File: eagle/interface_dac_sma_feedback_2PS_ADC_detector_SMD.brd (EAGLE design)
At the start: 158.8 x 119.4 mm, 26 parts

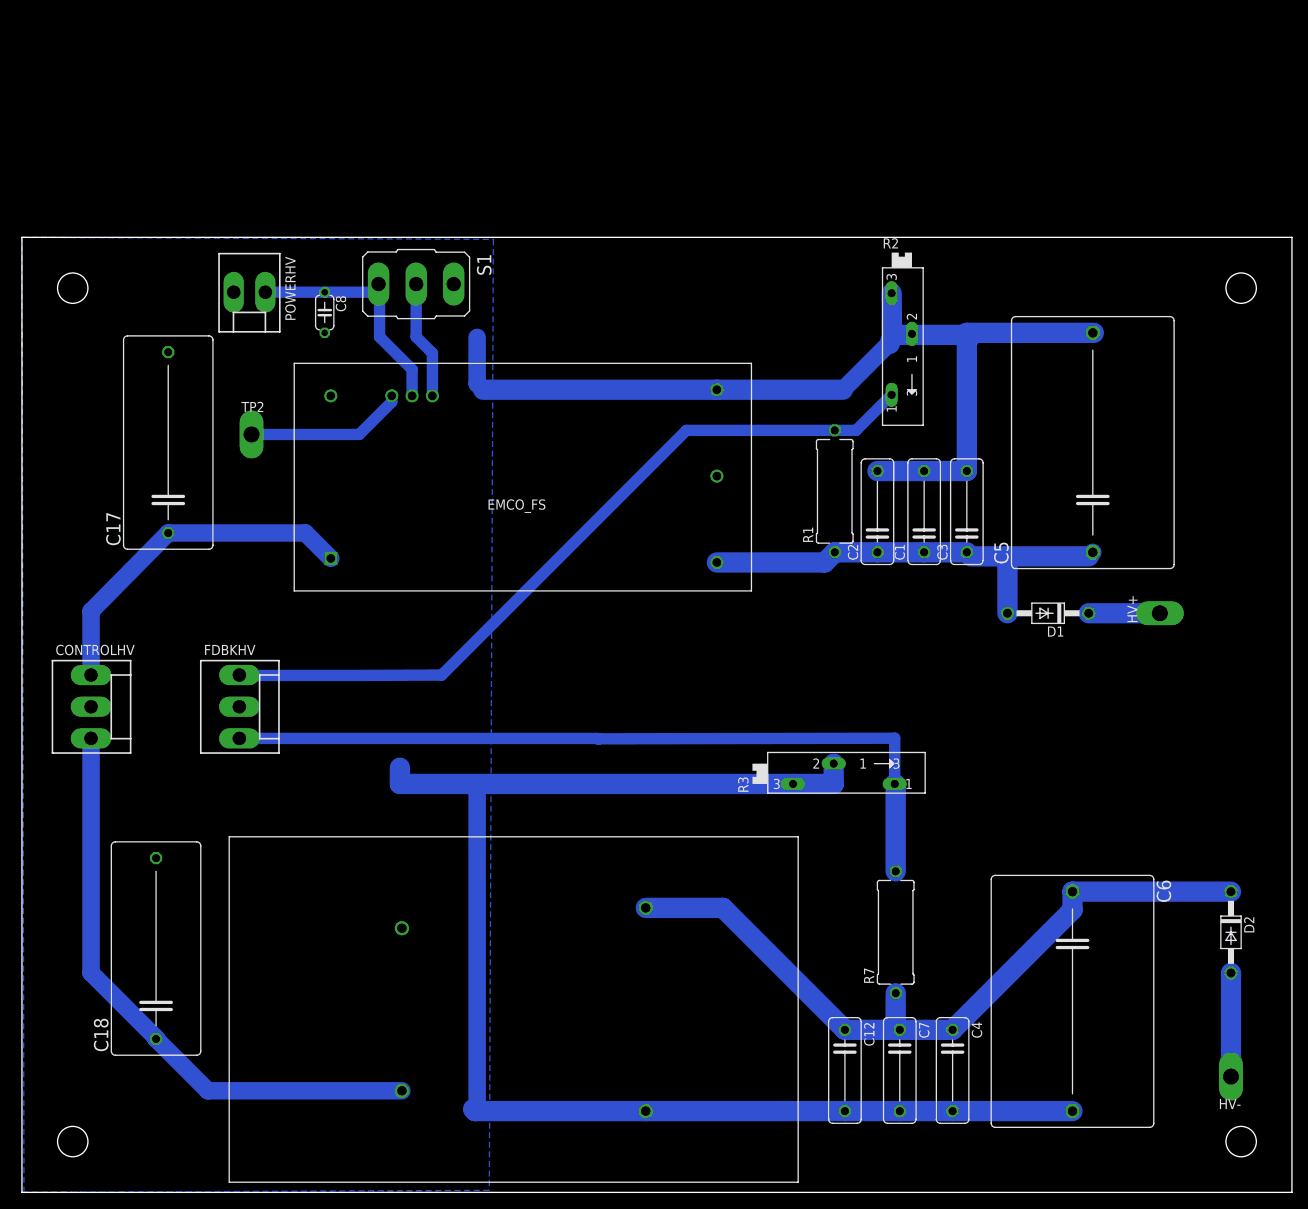
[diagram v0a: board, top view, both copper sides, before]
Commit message: Square wave one side/dc other
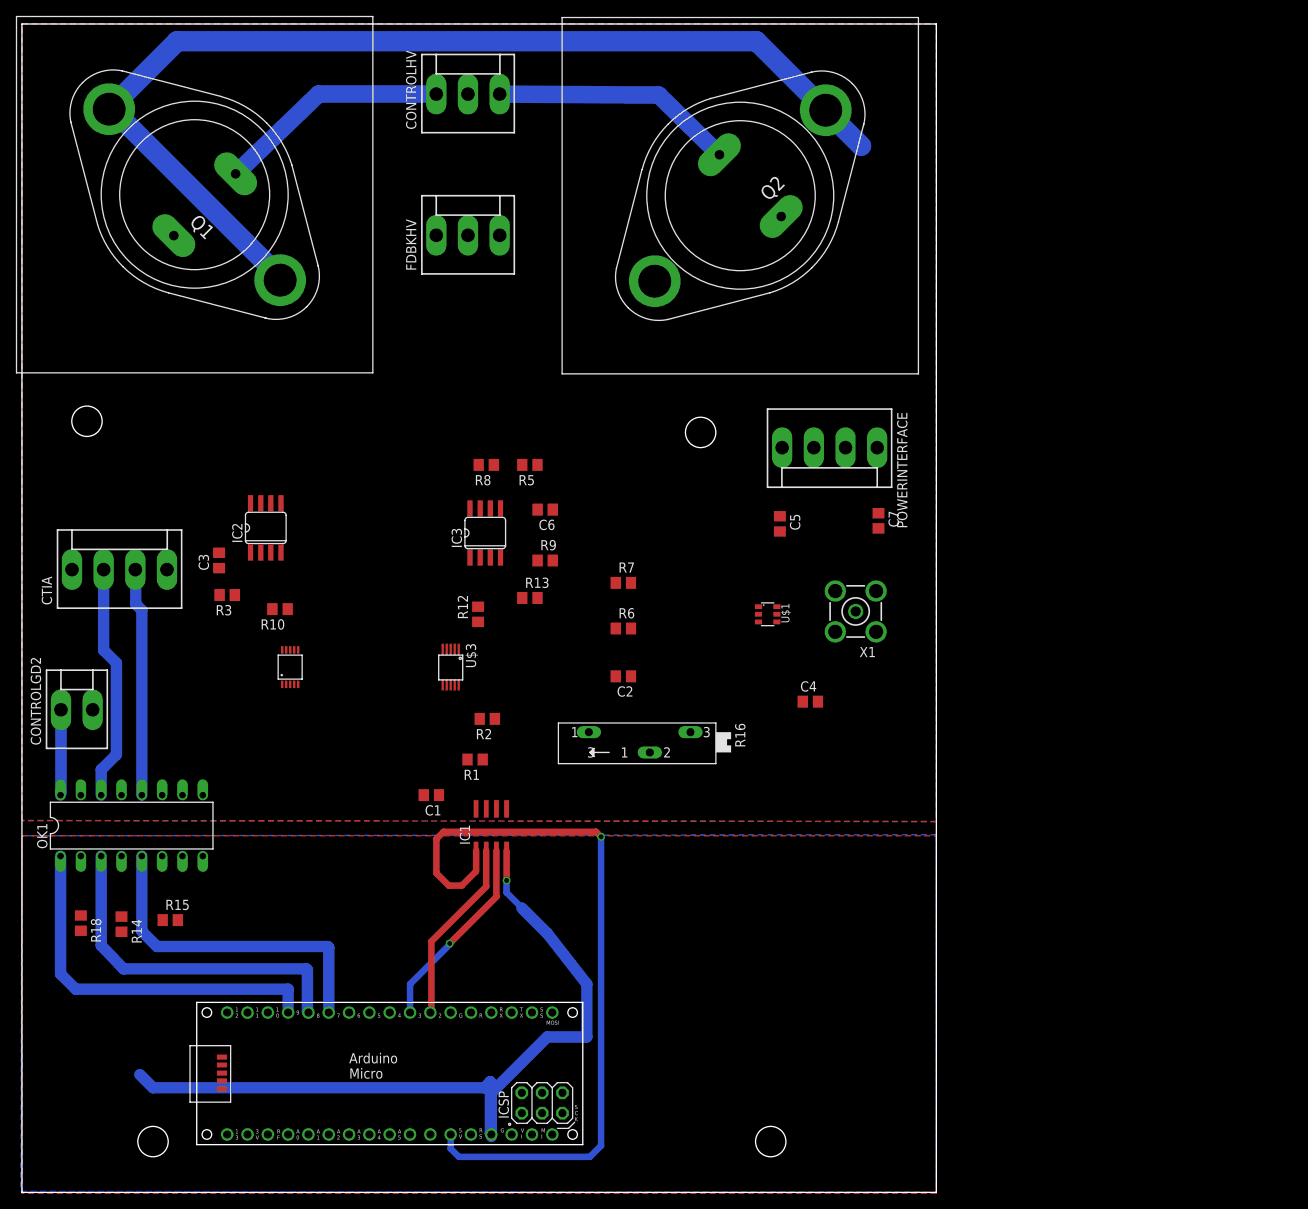
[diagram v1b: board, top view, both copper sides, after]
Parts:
- removed C12: .01u, rcl:C102-043X133
- removed C17, C18: .1u, rcl:C225-113X268
- removed C8: 10n, rcl:C050-024X044
- removed D1, D2: 1N4004, diode:DO41-10
- removed HV+, HV-: TPPAD1-20Y, testpad:P1-20Y
- removed POWERHV: (no value), con-molex:KK-156-2
- removed S1: (no value), switch:M9040P
- removed TP2: PTR1PAD1-20Y, testpad:P1-20Y
- added CONTROLGD2: (no value), con-molex:KK-156-2
- added CTIA, POWERINTERFACE: (no value), con-molex:KK-156-4
- added IC1: ISO1540SMD, texas:SOIC8
- added IC2, IC3: LT1352SA, linear-technology:SO08
- added OK1: PS2501", optocoupler:DIL16
- added PCB1: ARDUINO_MICRO, E14_Arduino_published:ARDUINO_MICRO
- added Q1, Q2: 2N3055, transistor-npn:TO3
- added R10, R12, R13, R6, R9: 10k, resistor:R0805
- added R14, R15, R18: 100, rcl:R0805
- added R16: 100k, pot:SP19L
- added R5, R8: 20k, resistor:R0805
- added U$3: ADS1015, texas:VSOP-10
- added X1: BU-SMA-V, con-coax:BU-SMA-V
- C1: value 1n -> 10n; device rcl:C102-043X133 -> rcl:C0805
- C2, C7: value 10p -> 10n; device rcl:C102-043X133 -> resistor:C0805
- C3: value .01u -> 10n; device rcl:C102-043X133 -> resistor:C0805
- C4: value 1n -> 10n; device rcl:C102-043X133 -> resistor:C0805
- C5, C6: value 1u -> 10n; device rcl:C275-205X316 -> resistor:C0805
- R1: value 2M -> 10k; device resistor:P0613/15 -> resistor:R0805
- R2, R3: value (none) -> 10k; device pot:SP19L -> resistor:R0805
- R7: value 2M -> 40k; device resistor:P0613/15 -> resistor:R0805
- U$1: value EMCO-FS10 -> LTC6992SMD; device dc-dc-converter:EMCO-FS -> linear-technology:SOT23-6
- U$2: value EMCO-F104PIN -> MCP4728; device dc-dc-converter:EMCO-F -> microchip:MSOP-10
- moved C3 93.7 mm to (24.6, 79.0)
- moved C6 90.1 mm to (65.4, 85.3), turned to 180 degrees
- moved CONTROLHV 89.9 mm to (55.8, 137.3), turned to 0 degrees
- moved R3 80.9 mm to (25.7, 74.7), turned to 180 degrees
- moved C1 71.1 mm to (51.2, 49.7), turned to 180 degrees
- moved R2 69.4 mm to (58.2, 59.2), turned to 180 degrees
- moved C7 68.8 mm to (107.1, 83.9)
- moved FDBKHV 65.5 mm to (55.8, 119.6), turned to 0 degrees
- moved U$1 59.3 mm to (93.2, 72.3), turned to 270 degrees
- moved R1 56.1 mm to (56.6, 54.1), turned to 180 degrees
- moved R7 55.4 mm to (75.2, 76.2), turned to 0 degrees
- moved U$2 54.8 mm to (33.5, 65.7), turned to 90 degrees
- moved C4 49.4 mm to (98.6, 61.3), turned to 0 degrees
- moved C5 40.4 mm to (94.7, 83.6), turned to 270 degrees
- moved C2 37.8 mm to (75.2, 64.5), turned to 180 degrees
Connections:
- removed net +5V: C8.1, POWERHV.1, S1.3, U$1.+5
- removed net N$10: TP2.TP, U$1.ALARM
- removed net N$15: C18.1, CONTROLHV.3, U$2.P$1
- new net +15V: C7.1, IC2.8, IC3.8, POWERINTERFACE.1, Q1.C, Q1.C/, Q2.C, Q2.C/
- new net -15V: C5.1, IC2.4, IC3.4, POWERINTERFACE.4
- new net A+5: IC1.1, PCB1.+5V
- new net AGND: IC1.4, PCB1.GND., R14.2, R15.2, R18.2
- new net CTIA: CTIA.4, U$3.AIN1
- new net D10: PCB1.D10
- new net D11: PCB1.D11
- new net D4: PCB1.D4
- new net D7: OK1.5, PCB1.D7
- new net D8: OK1.3, PCB1.D8
- new net ENSW2: CONTROLGD2.1, OK1.16
- new net N$12: R16.E, U$1.3
- new net N$14: IC3.7, R13.1, R8.2
- new net N$16: IC2.3, R10.2
- new net N$18: IC3.3, R12.2
- new net N$19: C3.2, IC2.1, Q1.B
- new net N$20: C6.1, R9.2
- new net N$21: C6.2, IC3.1, Q2.B
- new net N$23: IC3.6, R5.2, R8.1
- new net N$24: R10.1, U$2.P$9
- new net N$25: R12.1, U$2.P$7
- new net N$26: U$2.P$8
- new net N$7: OK1.2, R18.1
- new net PWM5: PCB1.D5
- new net PWM6: PCB1.D6
- new net PWM9: OK1.1, PCB1.D9
- new net RDBK1: FDBKHV.1, IC2.2, R3.1, U$3.AIN0
- new net RDBK3: IC3.2, R13.2, R9.1, U$3.AIN2
- new net RDBK4: C2.1, R6.2, R7.2, U$1.1, U$3.AIN3
- new net RESET: CTIA.3, OK1.12
- new net SAMPLE: CTIA.2, OK1.14
- new net SCL: IC1.3, PCB1.D3
- new net SCL_OUT: IC1.6, R2.1, U$2.P$2, U$3.SCL
- new net SDA: IC1.2, PCB1.D2
- new net SDA_OUT: IC1.7, R1.1, U$2.P$3, U$3.SDA
- new net VCC: C1.1, C4.1, IC1.8, POWERINTERFACE.2, R1.2, R2.2, U$1.5, U$2.P$1, U$3.VDD
- net GND: now also CONTROLGD2.2, CTIA.1, IC1.5, IC3.5, OK1.11, OK1.13, OK1.15, POWERINTERFACE.3, R16.A, R16.S, R6.1, U$1.2, U$1.4, U$2.P$10, U$2.P$4, U$3.ADDR, U$3.GND, X1.2, X1.3, X1.4, X1.5; no longer C12.2, C17.2, C18.2, C3.2, C6.2, C8.2, POWERHV.2, R2.E, R2.S, R3.E, R3.S, S1.1, U$1.-IN, U$1.-OUT, U$2.P$2, U$2.P$3
- net N$1: now also R7.1, U$2.P$6; no longer C1.1, C2.1, C3.1, C5.1, D1.A, R1.1, U$1.+OUT
- net N$13: now also U$1.6, X1.1; no longer C17.1, CONTROLHV.1, U$1.+IN
- net N$2: now also OK1.4, R14.1; no longer C12.1, C4.1, C6.1, C7.1, D2.C, R7.1, U$2.P$4
- net N$3: now also C3.1, R3.2; no longer FDBKHV.1, R1.2, R2.A
- net N$4: now also CONTROLHV.1, Q1.E; no longer D2.A, HV-.TP
- net N$5: now also CONTROLHV.3, Q2.E; no longer S1.2, U$1.DISABLE
- net N$6: now also OK1.6, R15.1; no longer D1.C, HV+.TP
- net N$8: now also R5.1; no longer R3.A, R7.2
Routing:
- net GND: track 340.8 -> 0.00 mm
- net +15V: track 0.00 -> 133.3 mm
- net AGND: track 0.00 -> 103.4 mm, vias 0 -> 1
- net N$8: track 98.9 -> 0.00 mm
- net N$3: track 96.1 -> 0.00 mm
- net A+5: track 0.00 -> 94.6 mm, vias 0 -> 1
- net N$2: track 92.5 -> 0.00 mm
- net N$15: track 74.5 -> 0.00 mm
- net N$1: track 55.0 -> 0.00 mm
- net PWM9: track 0.00 -> 46.9 mm
- net D8: track 0.00 -> 43.6 mm
- net N$13: track 43.4 -> 0.00 mm
- net D7: track 0.00 -> 41.7 mm
- net +5V: track 30.3 -> 0.00 mm
- net SAMPLE: track 0.00 -> 29.6 mm
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- added copper zone on layer 1, net AGND
- added copper zone on layer 16, net AGND
- added copper zone on layer 1, net GND
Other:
- board size 158.8 x 119.4 mm -> 114.3 x 146.1 mm
